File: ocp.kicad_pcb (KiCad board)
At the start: 2 copper layers, 54 x 54 mm, 13 parts, among them J1 ADS1115, J2 Screw_Terminal_01x03, J3 Screw_Terminal_01x02, U2 REF3033, U3 TL072

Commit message: Updated PCB
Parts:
- added C3: 1u, Capacitor_SMD:C_0402_1005Metric, F.Cu at (107.0, 125.0)
- added F1: 0.35A, Fuse:Fuse_1206_3216Metric, F.Cu at (109.8, 137.8)
- added H4: MountingHole, MountingHole:MountingHole_2.7mm_M2.5, F.Cu at (150.8, 156.5)
- added J4: MAX31865, Connector_PinHeader_2.54mm:PinHeader_1x08_P2.54mm_Vertical, F.Cu at (146.0, 109.2)
- added J5: UART, Connector_PinHeader_2.54mm:PinHeader_1x04_P2.54mm_Vertical, F.Cu at (145.8, 148.8)
- added R3: 100, Resistor_SMD:R_0603_1608Metric, F.Cu at (105.5, 125.5)
- added R4: 10k, Resistor_SMD:R_0603_1608Metric, B.Cu at (121.5, 117.4)
- added R5: 10k, Resistor_SMD:R_0603_1608Metric, B.Cu at (121.5, 114.2)
- added U4: TLV9062, Package_SO:TSSOP-8_4.4x3mm_P0.65mm, B.Cu at (120.5, 123.2)
- C1: footprint Capacitor_SMD:C_0603_1608Metric -> Capacitor_SMD:C_0402_1005Metric; moved to B.Cu
- C2: value 1u -> 2.2u; moved to B.Cu
- J1: value ADS1115 -> USB_C_Receptacle; footprint Connector_PinHeader_2.54mm:PinHeader_1x10_P2.54mm_Vertical -> Connector_USB:USB_C_Receptacle_G-Switch_GT-USB-7010ASV
- J2: value Screw_Terminal_01x03 -> Aviation_6Pin_GX16; footprint TerminalBlock_Phoenix:TerminalBlock_Phoenix_MKDS-1,5-3-5.08_1x03_P5.08mm_Horizontal -> TerminalBlock_Phoenix:TerminalBlock_Phoenix_MKDS-1,5-6-5.08_1x06_P5.08mm_Horizontal
- J3: value Screw_Terminal_01x02 -> ADS1115; footprint TerminalBlock_Phoenix:TerminalBlock_Phoenix_MKDS-1,5-2-5.08_1x02_P5.08mm_Horizontal -> Connector_PinHeader_2.54mm:PinHeader_1x10_P2.54mm_Vertical
- R1, R2: value 100 -> 5.1k; footprint Resistor_SMD:R_0603_1608Metric -> Resistor_SMD:R_0402_1005Metric
- U1: value ~ -> TPS60403DBV; footprint PCM_ESP32_30Pin:ESP32_30Pin -> Package_TO_SOT_SMD:SOT-23-5; moved to B.Cu
- U2: moved to B.Cu
- U3: value TL072 -> ESP32_30Pin; footprint Package_DIP:DIP-8_W7.62mm -> PCM_ESP32_30Pin:ESP32_30Pin
- moved H3 64.0 mm to (104.7, 156.5), turned to 0 degrees
- moved J3 52.7 mm to (109.5, 109.2), turned to 0 degrees
- moved R2 48.7 mm to (112.7, 138.0), turned to 90 degrees
- moved J2 40.4 mm to (115.2, 156.2), turned to 0 degrees
- moved R1 39.9 mm to (111.5, 138.0), turned to 90 degrees
- moved J1 39.3 mm to (103.1, 145.5), turned to -90 degrees
- moved U3 34.8 mm to (127.2, 122.5)
- moved C1 28.2 mm to (125.0, 122.7)
- moved U2 26.4 mm to (124.2, 111.9)
- moved H1 25.6 mm to (104.8, 104.0), turned to 180 degrees
- moved H2 25.4 mm to (150.8, 104.0), turned to 180 degrees
- moved C2 24.6 mm to (124.0, 116.2), turned to 90 degrees
- moved U1 20.5 mm to (125.0, 119.9), turned to -90 degrees
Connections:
- C1 pad 1: GND -> Net-(U1-C_{FLY+})
- C1 pad 2: Net-(J1-Pin_7) -> Net-(U1-C_{FLY-})
- C2 pad 1: Net-(J1-Pin_8) -> -3V3
- J2 pad 1: +5V -> GND
- J2 pad 2: GND -> /WE
- J2 pad 3: -5V -> unconnected-(J2-Pin_3-Pad3)
- J3 pad 1: GND -> +3V3
- J3 pad 2: /V- -> GND
- R1 pad 1: Net-(J1-Pin_7) -> Net-(J1-CC1)
- R1 pad 2: /RE -> GND
- R2 pad 1: Net-(J1-Pin_8) -> Net-(J1-CC2)
- R2 pad 2: /VREF -> GND
- U1 pad 1: +5V -> -3V3
- U1 pad 2: GND -> /VREF
- U1 pad 3: unconnected-(U1-GPIO13-Pad3) -> Net-(U1-C_{FLY-})
- U1 pad 4: unconnected-(U1-GPIO12-Pad4) -> GND
- U1 pad 5: unconnected-(U1-GPIO14-Pad5) -> Net-(U1-C_{FLY+})
- U3 pad 1: /RE -> +5V
- U3 pad 2: /RE -> GND
- U3 pad 3: /V- -> unconnected-(U3-GPIO13-Pad3)
- U3 pad 4: -5V -> unconnected-(U3-GPIO12-Pad4)
- U3 pad 5: GND -> unconnected-(U3-GPIO14-Pad5)
- U3 pad 6: Net-(U3B--) -> unconnected-(U3-GPIO27-Pad6)
- U3 pad 7: Net-(U3B--) -> unconnected-(U3-GPIO26-Pad7)
- U3 pad 8: +5V -> unconnected-(U3-GPIO25-Pad8)
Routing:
- net +5V: track 66.1 -> 0.00 mm
- net +3V3: track 61.6 -> 0.00 mm
- net -5V: track 45.9 -> 0.00 mm, vias 2 -> 0
- net /RE: track 42.9 -> 0.00 mm
- net /SCL: track 38.3 -> 0.00 mm, vias 2 -> 0
- net /SDA: track 33.5 -> 0.00 mm
- net /V-: track 21.7 -> 0.00 mm
- net GND: track 7.61 -> 0.00 mm, vias 2 -> 0
- net Net-(J1-Pin_7): track 6.49 -> 0.00 mm
- net Net-(J1-Pin_8): track 6.48 -> 0.00 mm
- net Net-(U3B--): track 2.54 -> 0.00 mm
- net /VREF: track 2.22 -> 0.00 mm
- net (no net): vias 2 -> 0
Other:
- board size 54 x 54 mm -> 54 x 62.2 mm
- board text added: "ADS1115"
- board text added: "Indriya Sensotech Private Limited"
- board text added: "MAX31865"
- board text added: "OCP Meter v2.0 Kishan"
- board text added: "RE WE"
- board text added: "V TX RX G"
- board text added: "VIN"
- board text removed: "+5V"
- board text removed: "-5V"
- board text removed: "Indriya Sensotech Private Limited OCP Meter v1.0 Kishan"
- board text removed: "RE"
- board text removed: "WE"

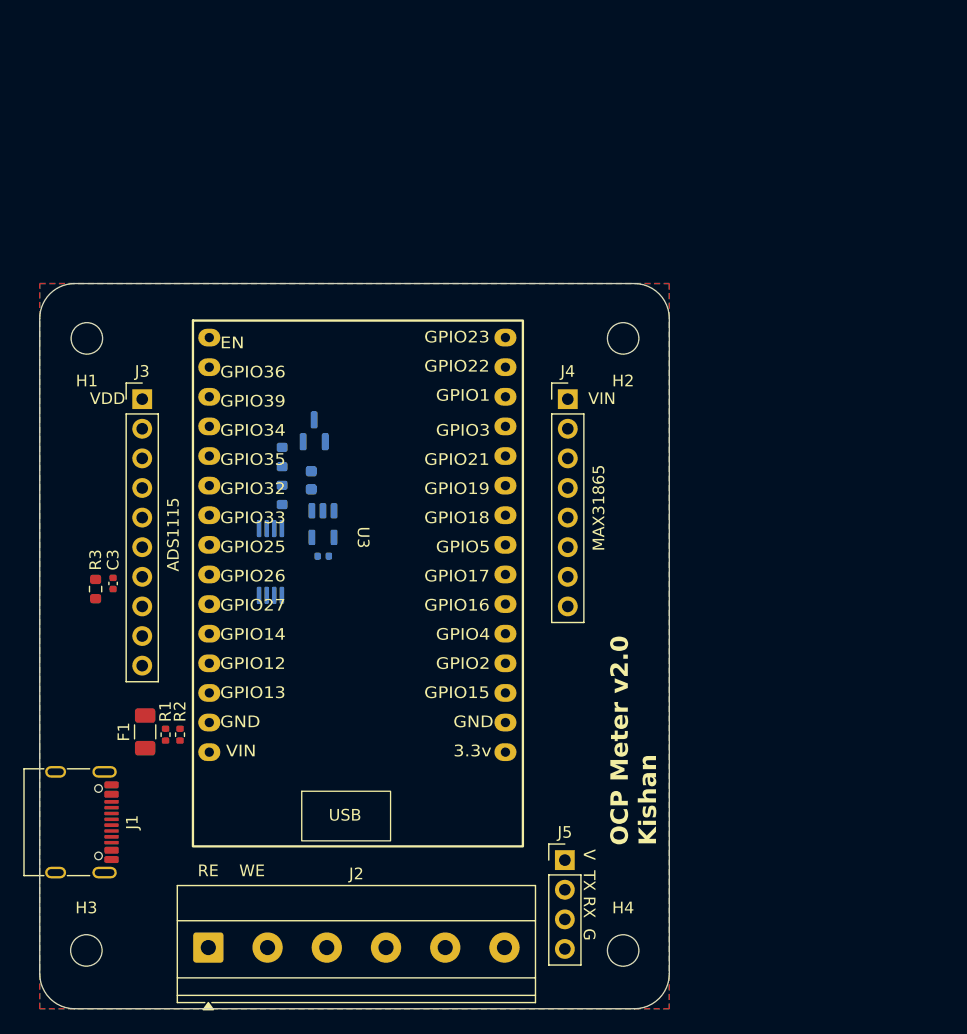
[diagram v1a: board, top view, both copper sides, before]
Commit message: Finished routing PCB
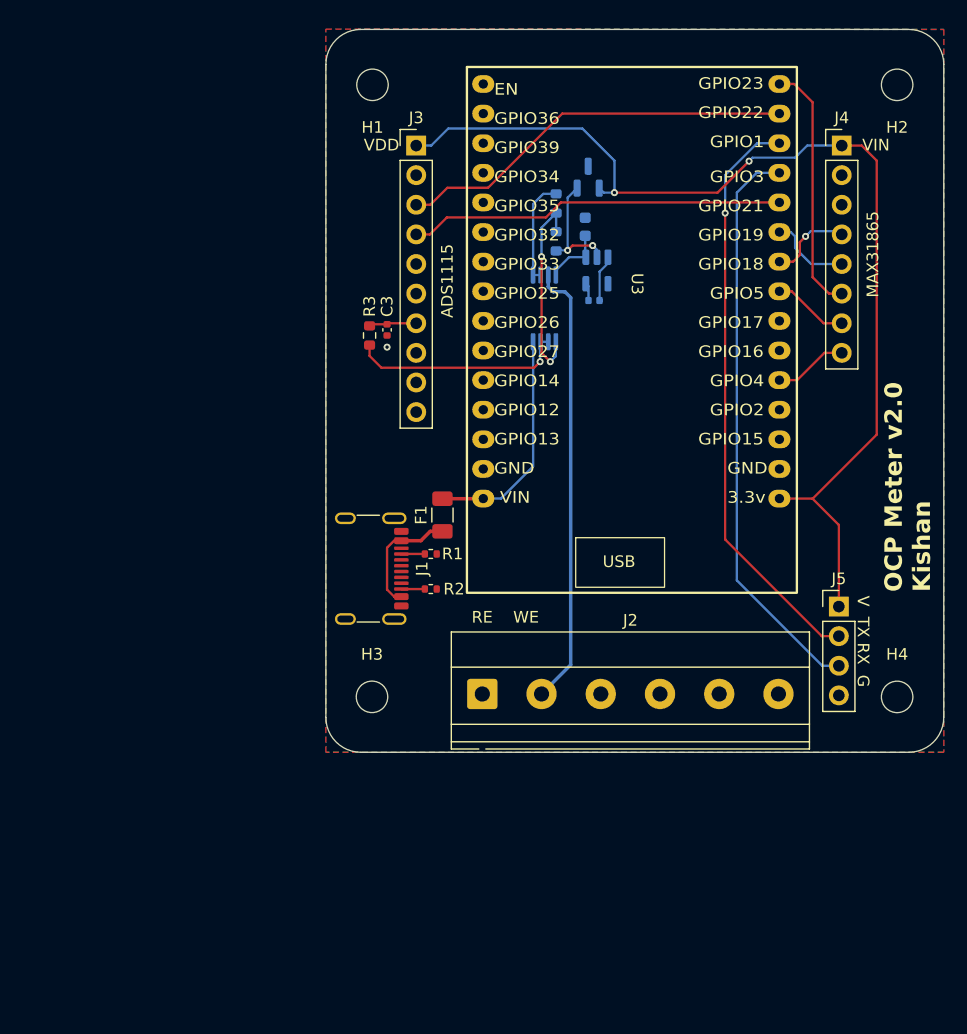
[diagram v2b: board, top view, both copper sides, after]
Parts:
- moved J1 33.0 mm to (128.0, 123.8)
- moved H3 32.8 mm to (129.2, 134.7)
- moved H1 32.8 mm to (129.2, 82.2)
- moved C2 32.0 mm to (147.5, 94.4)
- moved C3 32.0 mm to (130.5, 103.3)
- moved H2 32.0 mm to (174.2, 82.2)
- moved H4 32.0 mm to (174.2, 134.8)
- moved J3 32.0 mm to (133.0, 87.5)
- moved J4 32.0 mm to (169.5, 87.5)
- moved J5 32.0 mm to (169.2, 127.0)
- moved R3 32.0 mm to (129.0, 103.8)
- moved R4 32.0 mm to (145.0, 95.7)
- moved R5 32.0 mm to (145.0, 92.4)
- moved U1 32.0 mm to (148.5, 98.2)
- moved U2 32.0 mm to (147.8, 90.2)
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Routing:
- net +3V3: track 0.00 -> 92.0 mm, vias 0 -> 2
- net /TX: track 0.00 -> 50.2 mm, vias 0 -> 1
- net /RX: track 0.00 -> 49.4 mm
- net /WE: track 0.00 -> 38.4 mm
- net /SCL: track 0.00 -> 34.4 mm
- net /SDA: track 0.00 -> 32.3 mm
- net /MAX31865_SDI: track 0.00 -> 21.6 mm
- net +5V: track 0.00 -> 19.6 mm
- net /VADC_OUT: track 0.00 -> 18.7 mm, vias 0 -> 1
- net Net-(U4B-+): track 0.00 -> 17.1 mm, vias 0 -> 2
- net Net-(F1-Pad1): track 0.00 -> 10.4 mm
- net /VREF: track 0.00 -> 10.1 mm, vias 0 -> 2
- net /RE: track 0.00 -> 9.07 mm
- net /MAX31865_CLK: track 0.00 -> 7.19 mm, vias 0 -> 1
- net /MAX31865_SDO: track 0.00 -> 7.07 mm
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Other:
- board size 54 x 62.2 mm -> 53 x 62 mm

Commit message: Updated PCB
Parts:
- added C4: 1u, Capacitor_SMD:C_0402_1005Metric, B.Cu at (149.4, 95.5)
- F1: value 0.35A -> 0.75A
- R4, R5: value 10k -> 10k 0.1%
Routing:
- net /VREF: track 10.1 -> 11.9 mm
